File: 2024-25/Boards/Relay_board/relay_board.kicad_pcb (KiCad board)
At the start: 2 copper layers, 41.9 x 37.3 mm, 18 parts, among them J2 043045-1212, K1 1462043-4, K2 1462043-4, K3 1462043-4, K4 1462043-4, Q1 PJA3412_R1_00001, Q2 PJA3412_R1_00001, Q3 PJA3412_R1_00001, U1 HEF4049B

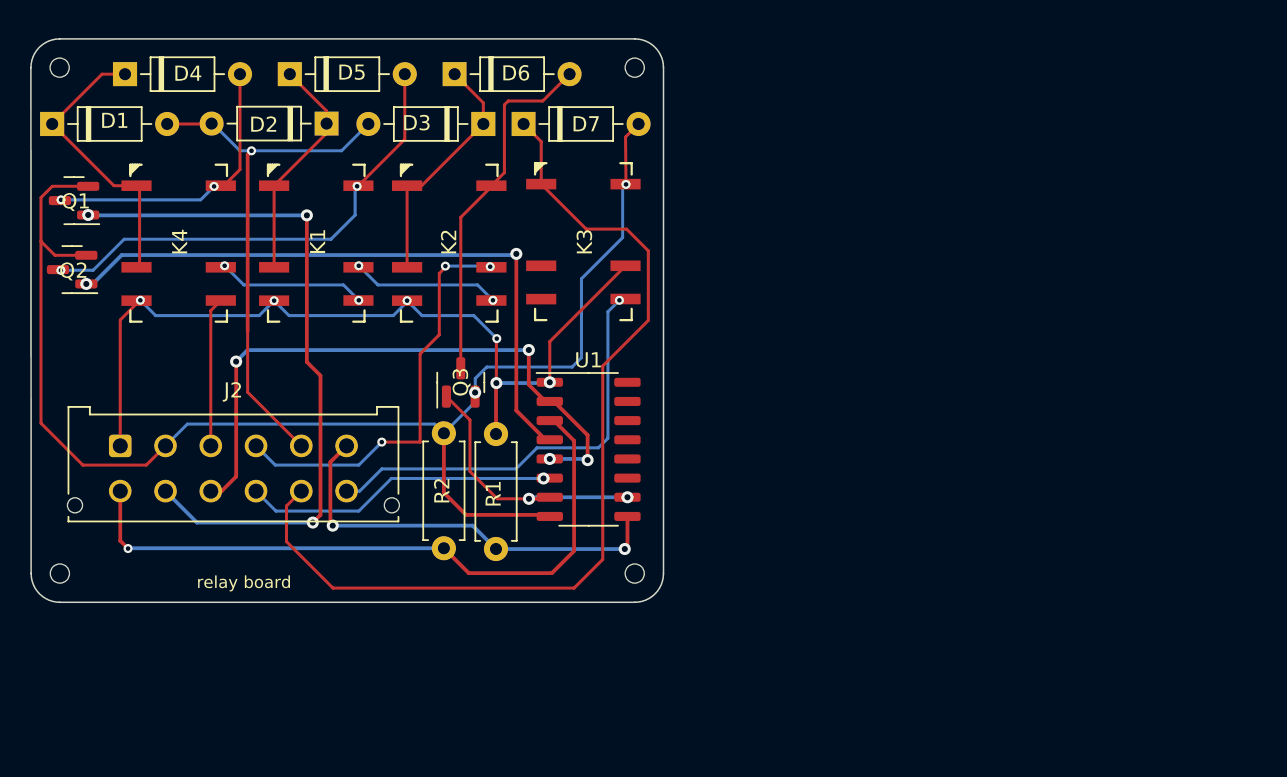
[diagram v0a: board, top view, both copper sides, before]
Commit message: accum and HV box schm
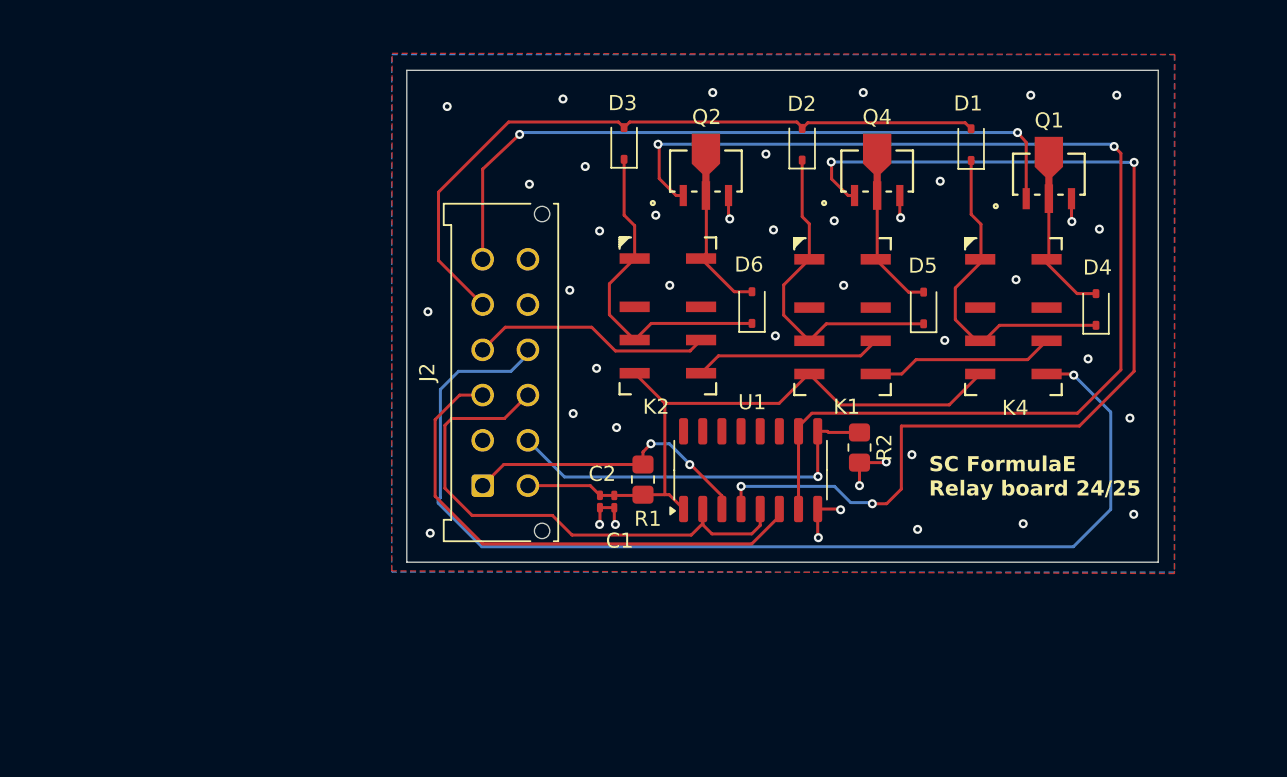
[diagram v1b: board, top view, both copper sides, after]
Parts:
- removed D7: 1N4148, Diode_THT:D_DO-35_SOD27_P7.62mm_Horizontal
- removed K3: 1462043-4, Relay_SMD:Relay_DPDT_AXICOM_IMSeries_JLeg
- removed Q3: PJA3412_R1_00001, Package_TO_SOT_SMD:SOT-23
- added C1: 1uF, Capacitor_SMD:C_0201_0603Metric_Pad0.64x0.40mm_HandSolder, F.Cu at (137.1, 109.6)
- added C2: .1uF, Capacitor_SMD:C_0201_0603Metric_Pad0.64x0.40mm_HandSolder, F.Cu at (136.1, 109.6)
- added Q4: VN3205N3-G, VN3205N8-G:TO-243AA_MCH, F.Cu at (154.5, 87.7)
- D1, D2, D3, D4, D5, D6: value 1N4148 -> 1N4148WX-TP; footprint Diode_THT:D_DO-35_SOD27_P7.62mm_Horizontal -> Diode_SMD:D_SOD-323
- Q1, Q2: value PJA3412_R1_00001 -> VN3205N3-G; footprint Package_TO_SOT_SMD:SOT-23 -> VN3205N8-G:TO-243AA_MCH
- R1, R2: value 2.2k -> 10k; footprint Resistor_THT:R_Axial_DIN0207_L6.3mm_D2.5mm_P7.62mm_Horizontal -> Resistor_SMD:R_0805_2012Metric_Pad1.20x1.40mm_HandSolder
- moved D4 66.2 mm to (169.0, 96.9), turned to 90 degrees
- moved Q1 64.6 mm to (165.9, 87.9), turned to 0 degrees
- moved D1 60.9 mm to (160.7, 86.0), turned to 90 degrees
- moved K4 55.5 mm to (163.5, 97.3)
- moved D5 44.8 mm to (157.6, 96.8), turned to 90 degrees
- moved Q2 42.5 mm to (143.1, 87.7), turned to 0 degrees
- moved K1 35.2 mm to (152.2, 97.3)
- moved D2 31.5 mm to (149.5, 85.9), turned to 90 degrees
- moved R2 28.3 mm to (153.3, 106.0), turned to -90 degrees
- moved D6 25.1 mm to (146.2, 96.8), turned to 90 degrees
- moved J2 24.2 mm to (128.3, 108.5), turned to 90 degrees
- moved K2 15.3 mm to (140.6, 97.3)
- moved U1 10.8 mm to (146.1, 107.5), turned to 90 degrees
- moved R1 10.8 mm to (139.0, 108.2), turned to -90 degrees
- moved D3 9.42 mm to (137.7, 85.9), turned to 90 degrees
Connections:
- net SW renamed Reset
- J2 pad 1: +12V -> IMD Fault
- J2 pad 10: BMS_indicator -> SDC 1
- J2 pad 11: BMS_power -> unconnected-(J2-Pin_11-Pad11)
- J2 pad 12: BMS_charge -> unconnected-(J2-Pin_12-Pad12)
- J2 pad 3: SDC 1 -> BMS_indicator
- J2 pad 6: BMS Fault -> BSPD Fault
- J2 pad 7: IMD Fault -> +12V
- J2 pad 8: BSPD Fault -> BMS Fault
- Q1 pad 2: GND -> /Drain_BSPD
- Q1 pad 3: /Drain_BSPD -> GND
- Q2 pad 1: Net-(Q2-G) -> /BMS_relay_drive
- Q2 pad 2: GND -> /Drain_BMS
- Q2 pad 3: /Drain_IMD -> GND
- R1 pad 1: BMS Fault -> IMD Fault
- R2 pad 1: IMD Fault -> BMS Fault
- U1 pad 10: Net-(Q3-G) -> /BMS_relay_drive
- U1 pad 4: Net-(Q2-G) -> /IMD_relay_drive
- U1 pad 7: Net-(Q3-G) -> /BMS_relay_drive
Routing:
- net /BMS_relay_drive: track 0.00 -> 78.1 mm, vias 0 -> 2
- net GND: track 91.7 -> 16.2 mm, vias 2 -> 41
- net /IMD_relay_drive: track 0.00 -> 71.9 mm, vias 0 -> 4
- net SDC 1: track 9.91 -> 73.4 mm, vias 0 -> 1
- net BMS_power: track 61.9 -> 0.00 mm
- net Net-(Q2-G): track 42.7 -> 0.00 mm, vias 2 -> 0
- net BMS_charge: track 28.2 -> 0.00 mm, vias 1 -> 0
- net IMD Fault: track 44.4 -> 19.8 mm, vias 1 -> 2
- net /Drain_IMD: track 31.8 -> 8.02 mm, vias 2 -> 0
- net Net-(Q3-G): track 18.3 -> 0.00 mm, vias 2 -> 0
- net /Drain_BMS: track 23.8 -> 8.39 mm
- net BMS_indicator: track 20.9 -> 34.3 mm, vias 1 -> 0
- net +12V: track 56.3 -> 43.3 mm, vias 6 -> 0
- net SDC 2: track 27.6 -> 16.0 mm, vias 3 -> 0
- net Reset: track 36.0 -> 46.7 mm, vias 1 -> 0
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- added copper zone on B.Cu, net GND
- added copper zone on F.Cu, net GND
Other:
- board size 41.9 x 37.3 mm -> 49.8 x 32.6 mm
- board text added: "SC FormulaE Relay board 24/25"
- board text removed: "relay board"

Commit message: checkbox schm
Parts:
- removed C2: .1uF, Capacitor_SMD:C_0201_0603Metric_Pad0.64x0.40mm_HandSolder
- added H1: MountingHole, MountingHole:MountingHole_4.3mm_M4, F.Cu at (120.5, 84.7)
- added H2: MountingHole, MountingHole:MountingHole_4.3mm_M4, F.Cu at (120.3, 113.1)
- added H3: MountingHole, MountingHole:MountingHole_4.3mm_M4, F.Cu at (163.4, 113.4)
- added H4: MountingHole, MountingHole:MountingHole_4.3mm_M4, F.Cu at (106.5, 123.7)
- C1: footprint Capacitor_SMD:C_0201_0603Metric_Pad0.64x0.40mm_HandSolder -> Capacitor_SMD:C_0805_2012Metric_Pad1.18x1.45mm_HandSolder
- moved C1 0.76 mm to (136.7, 110.2)
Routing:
- net GND: track 16.2 -> 14.8 mm, vias 41 -> 40

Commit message: full schem
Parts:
- moved H4 78.3 mm to (174.4, 84.7)
- moved H3 11.0 mm to (174.4, 112.6)
- moved H2 0.50 mm to (120.3, 112.6)
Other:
- board size 49.8 x 32.6 mm -> 64.6 x 38.9 mm
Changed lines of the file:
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@@
 	(footprint "MountingHole:MountingHole_4.3mm_M4"
 		(layer "F.Cu")
-		(at 163.45 113.4)
+		(at 174.45 112.6)
 		(descr "Mounting Hole 4.3mm, no annular, M4")
 		(tags "mounting hole 4.3mm no annular m4")
@@
 	(footprint "MountingHole:MountingHole_4.3mm_M4"
 		(layer "F.Cu")
-		(at 106.55 123.7)
+		(at 174.45 84.7)
 		(descr "Mounting Hole 4.3mm, no annular, M4")
 		(tags "mounting hole 4.3mm no annular m4")
@@
 	(footprint "MountingHole:MountingHole_4.3mm_M4"
 		(layer "F.Cu")
-		(at 120.35 113.1)
+		(at 120.35 112.6)
 		(descr "Mounting Hole 4.3mm, no annular, M4")
 		(tags "mounting hole 4.3mm no annular m4")
@@
 	)
 	(gr_rect
-		(start 123.325 81.025)
-		(end 173.125 113.625)
+		(start 115.05 79)
+		(end 179.65 117.9)
 		(stroke
 			(width 0.05)
@@
 		(polygon
 			(pts
-				(xy 174.2 114.375) (xy 122.325 114.2) (xy 122.35 79.9) (xy 174.225 79.975) (xy 174.2 114.2)
+				(xy 174.5 117.375) (xy 115.525 117.5) (xy 115.35 79.3) (xy 179.325 79.475) (xy 179.45 117.4)
 			)
 		)
@@
 		(polygon
 			(pts
-				(xy 122.324476 114.283114) (xy 122.324476 79.983114) (xy 174.199476 79.983114) (xy 174.199476 114.283114)
+				(xy 115.424476 117.883114) (xy 115.35 79.5) (xy 179.05 79.7) (xy 178.999476 117.583114)
 			)
 		)
